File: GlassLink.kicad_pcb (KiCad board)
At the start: 2 copper layers, 37 x 13 mm, 37 parts, among them J1 USB_C_Receptacle_USB2.0, J2 FTSH-105-01-F-DV-K, SW1 SW_Push, U1 SN65220, U2 AP2204K-3.3, U3 LPC11U35FHI33_501, Y1 ECS-120-20-30B-TR

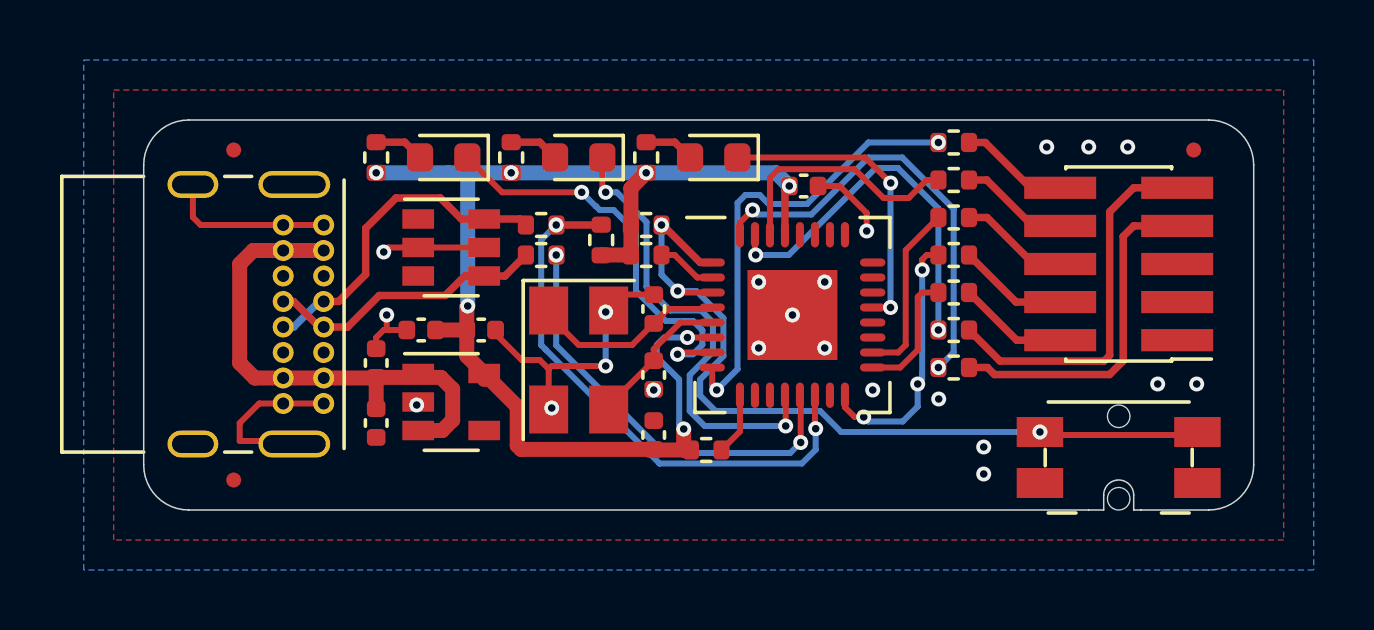
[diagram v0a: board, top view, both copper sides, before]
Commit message: Pull TGT Reset to the TGT VCC instead of the prog VCC
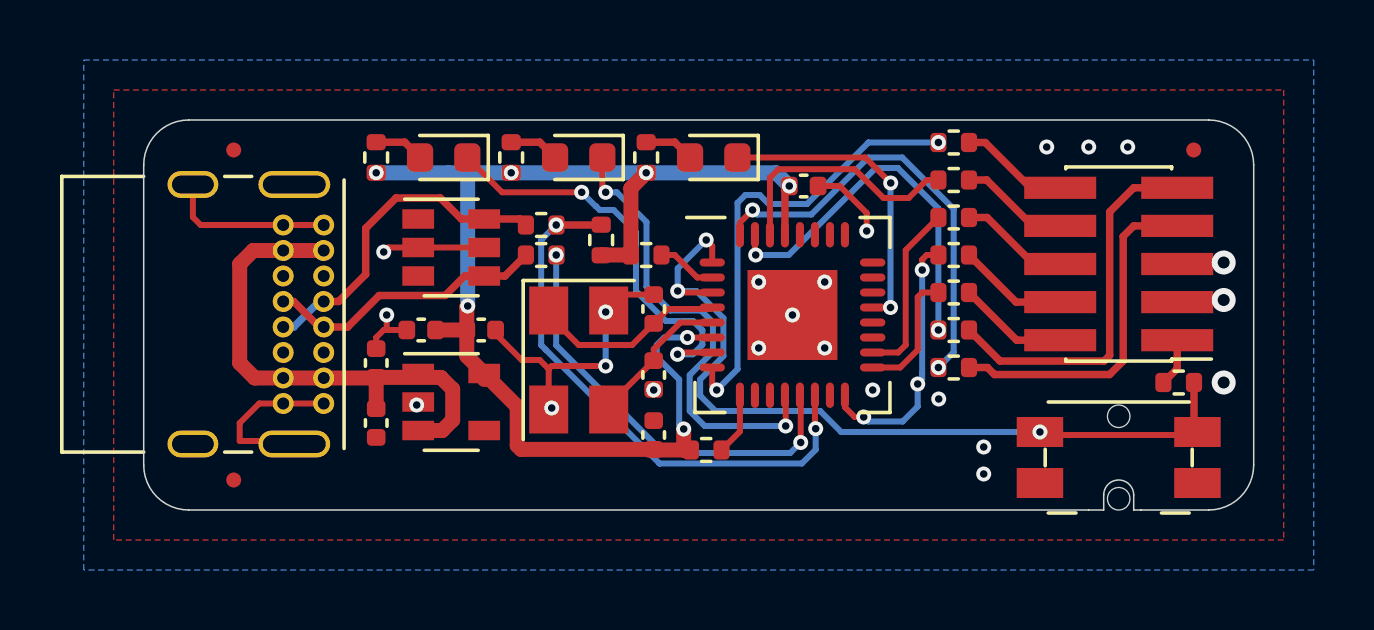
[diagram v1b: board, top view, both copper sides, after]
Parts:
- moved R1 18.5 mm to (34.5, -4.25)
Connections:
- J2 pad 1: Net-(J2-Pad1) -> /VTARGET
- R1 pad 1: +3V3 -> /VTARGET
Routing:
- net /VTARGET: track 0.00 -> 1.60 mm
- net GND: vias 22 -> 23

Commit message: Adding Glassboard G logo
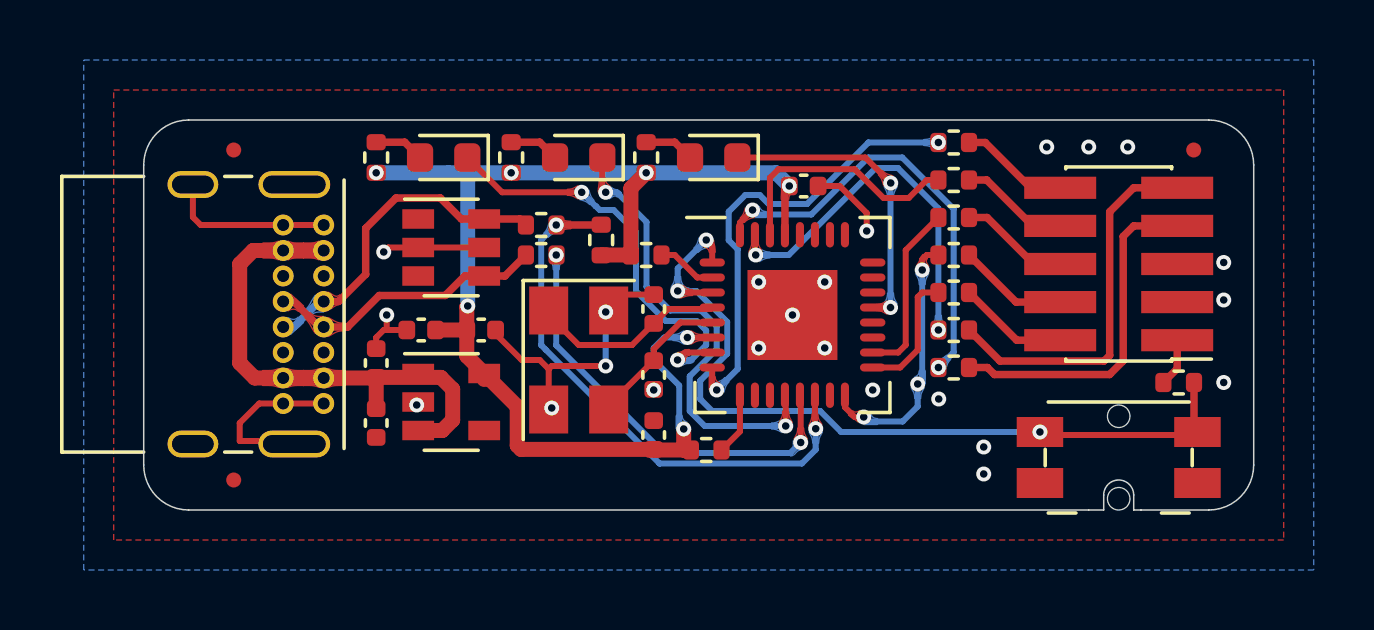
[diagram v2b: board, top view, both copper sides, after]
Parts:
- added G***: LOGO, GlassLink:GlassboardG_7x7, B.Cu at (31.0, -6.50)
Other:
- board text added: "r0.5"
- board text removed: "R0.5"

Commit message: Pulling TGT_RESET to DAPLink 3.3V rail
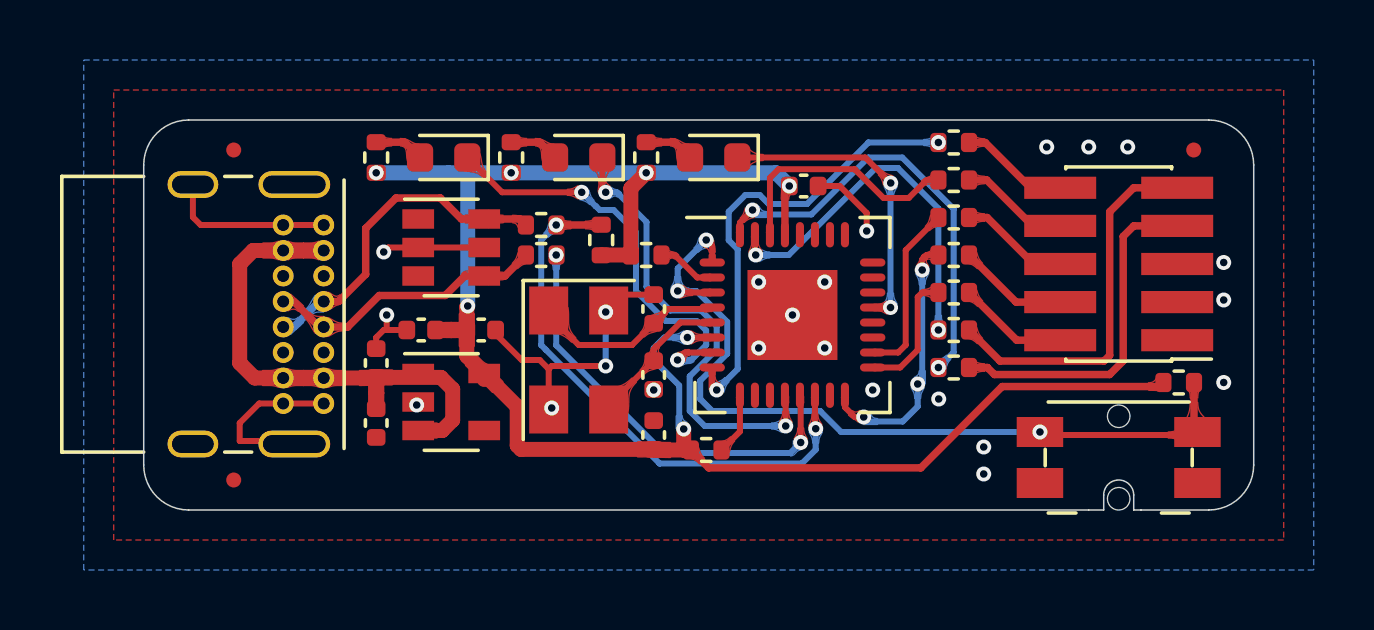
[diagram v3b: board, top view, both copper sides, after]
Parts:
- removed G***: LOGO, GlassLink:GlassboardG_7x7
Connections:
- R1 pad 1: /VTARGET -> +3V3
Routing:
- net +3V3: track 42.3 -> 59.5 mm
- net /VTARGET: track 1.60 -> 0.00 mm
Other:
- board text added: "r0.6"
- board text removed: "r0.5"

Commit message: Fixing trace on top layer behind Glasslabs label
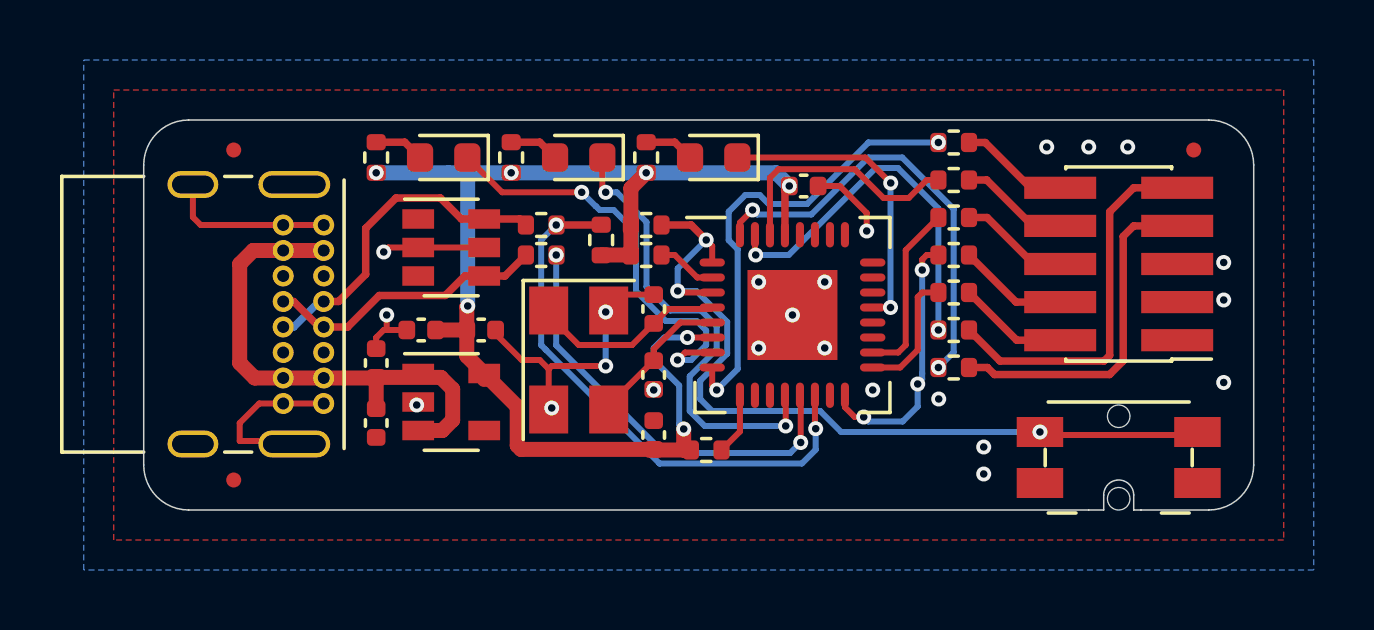
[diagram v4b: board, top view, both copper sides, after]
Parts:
- moved R1 18.5 mm to (16.8, -9.50)
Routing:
- net +3V3: track 59.5 -> 42.3 mm
